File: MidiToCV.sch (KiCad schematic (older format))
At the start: 11 parts, among them J17 67997-216, J18 Conn_01x02_Female, J19 Conn_01x02_Female, Q1 LP2954IT_NOPB, U2 MAX6102, U4 6N138

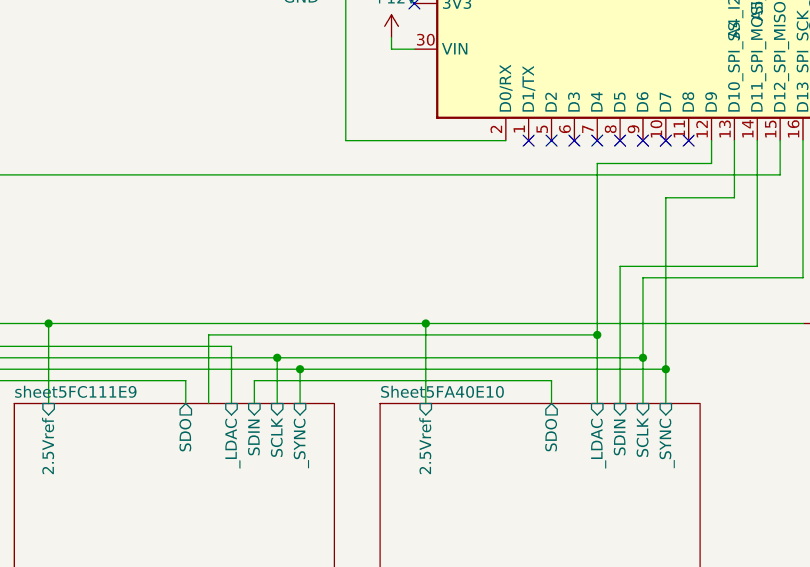
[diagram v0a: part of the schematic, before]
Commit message: ladc_ bug fix
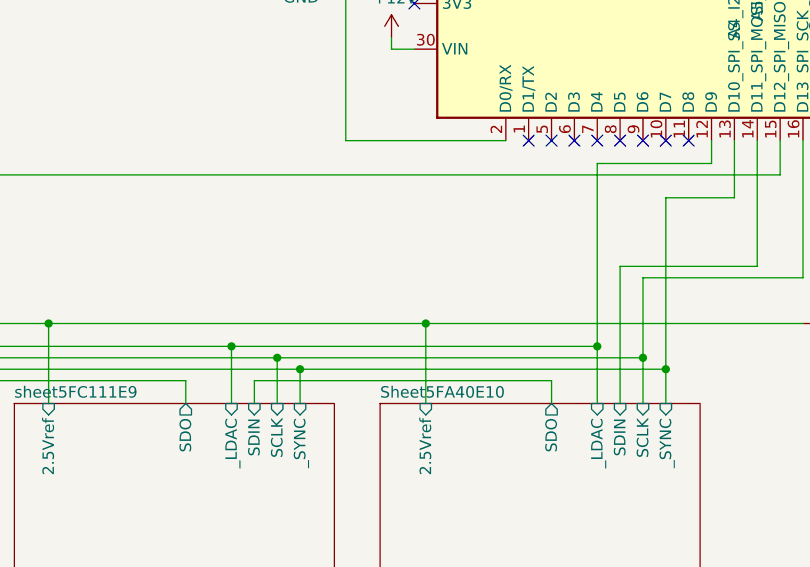
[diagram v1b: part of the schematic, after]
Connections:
- net sheet5FC111E9/_LDAC is gone; now on net Sheet5FA40E10/_LDAC: J17.7, J17.8
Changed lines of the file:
@@
-$EndSheet
-$Sheet
-S 6000 4050 1400 2150
-U 5FC111F1
-F0 "sheet5FC111E9" 50
-F1 "file5FA40E10.sch" 50
-F2 "_SYNC" I T 7250 4050 50
-F3 "SCLK" I T 7150 4050 50
-F4 "SDIN" I T 7050 4050 50
-F5 "_LDAC" I T 6950 4050 50
-F6 "SDO" O T 6750 4050 50
-F7 "2.5Vref" I T 6150 4050 50
 $EndSheet
 $Sheet
@@
 Connection ~ 5350 3800
 Wire Wire Line
-	8550 3750 6850 3750
-Wire Wire Line
-	6850 3750 6850 4050
-Wire Wire Line
-	8550 3750 8550 4050
+	8550 3800 6950 3800
+Wire Wire Line
+	8550 3800 8550 4050
 $Comp
 L power:GND #PWR019
@@
 Connection ~ 8850 3900
 Wire Wire Line
-	8550 3750 8550 3000
-Connection ~ 8550 3750
+	8550 3800 8550 3000
+Connection ~ 8550 3800
 Wire Wire Line
 	9150 2900 9150 3150
@@
 NoConn ~ 7750 2200
 NoConn ~ 7750 2300
+$Sheet
+S 6000 4050 1400 2150
+U 5FC111F1
+F0 "sheet5FC111E9" 50
+F1 "file5FA40E10.sch" 50
+F2 "_SYNC" I T 7250 4050 50
+F3 "SCLK" I T 7150 4050 50
+F4 "SDIN" I T 7050 4050 50
+F5 "_LDAC" I T 6950 4050 50
+F6 "SDO" O T 6750 4050 50
+F7 "2.5Vref" I T 6150 4050 50
+$EndSheet
+Connection ~ 6950 3800
 $EndSCHEMATC
